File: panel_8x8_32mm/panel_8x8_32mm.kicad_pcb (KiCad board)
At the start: 2 copper layers, 32 x 32 mm, 17 parts, among them IC1 ATMEGA168-A, P1 CONN_8, P2 CONN_8, U1 ULN2804A, X1 CR

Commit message: consistent file naming
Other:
- board text added: "https://reiserlab.github.io/ Modular-LED-Display/"
- board text added: "panel 8x8 32mm v1.4 (2021)"
- board text removed: "Flypanel v1.3 (2012)"
- board text removed: "IO Rodeo Inc. (626) 793-8284"
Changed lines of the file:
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@@
     (visible_elements FFFFFF7F)
     (pcbplotparams
-      (layerselection 0x00030_ffffffff)
+      (layerselection 0x010f0_ffffffff)
       (usegerberextensions true)
       (usegerberattributes true)
@@
       (outputformat 1)
       (mirror false)
-      (drillshape 1)
+      (drillshape 0)
       (scaleselection 1)
-      (outputdirectory "gerber_v1p3/"))
+      (outputdirectory "production_v1/"))
   )
   (net 0 "")
@@
   (gr_line (start 99.9998 68.00088) (end 132.00126 68.00088) (angle 90) (layer Edge.Cuts) (width 0.381))
   (gr_line (start 99.9998 99.9998) (end 99.9998 68.00088) (angle 90) (layer Edge.Cuts) (width 0.381))
-  (gr_text "IO Rodeo Inc. (626) 793-8284" (at 100.89896 83.10118 90) (layer B.SilkS)
+  (gr_text "https://reiserlab.github.io/\nModular-LED-Display/" (at 116.52 70.55) (layer B.SilkS)
     (effects (font (size 1.00076 1.00076) (thickness 0.20066)) (justify mirror))
   )
-  (gr_text "Flypanel v1.3 (2012)" (at 116.0018 69.99986) (layer B.SilkS)
+  (gr_text "panel 8x8 32mm v1.4 (2021)" (at 101.3 84.52 90) (layer B.SilkS)
     (effects (font (size 1.00076 1.00076) (thickness 0.20066)) (justify mirror))
   )

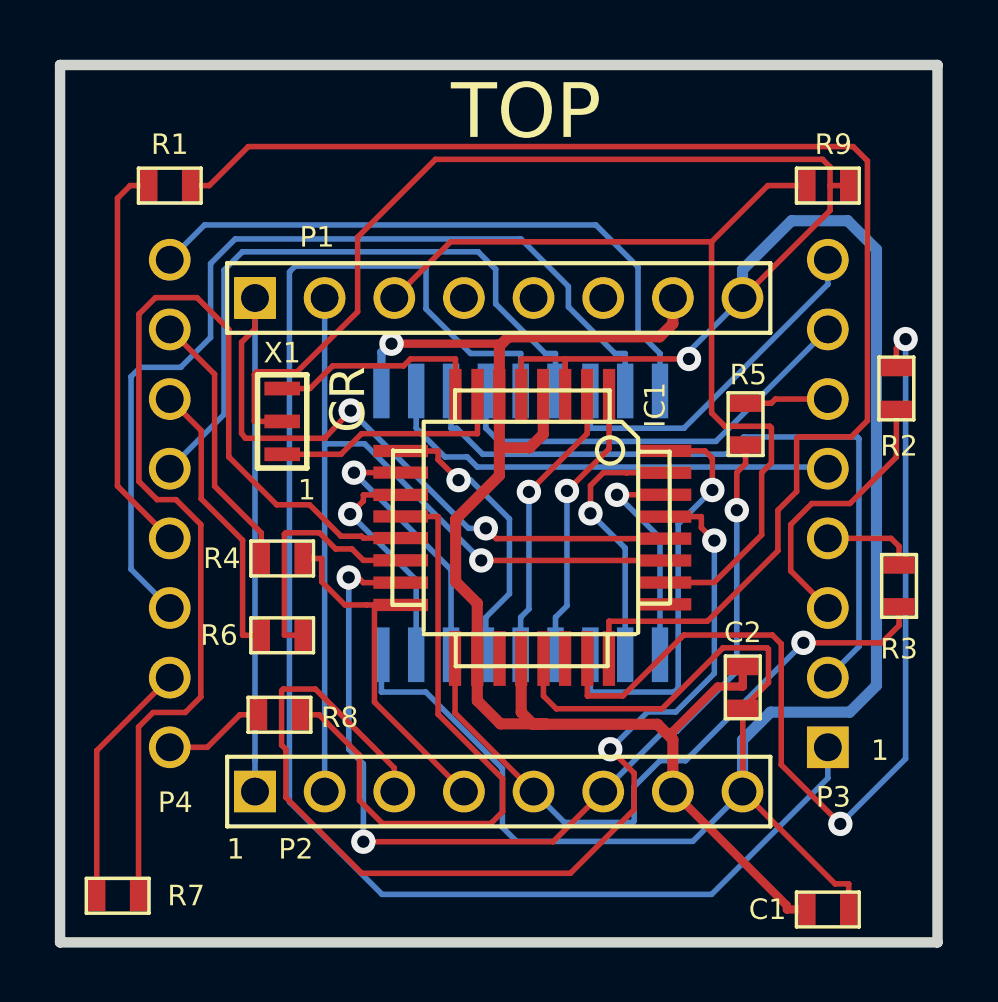
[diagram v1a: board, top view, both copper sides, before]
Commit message: migrate to KiCad 6
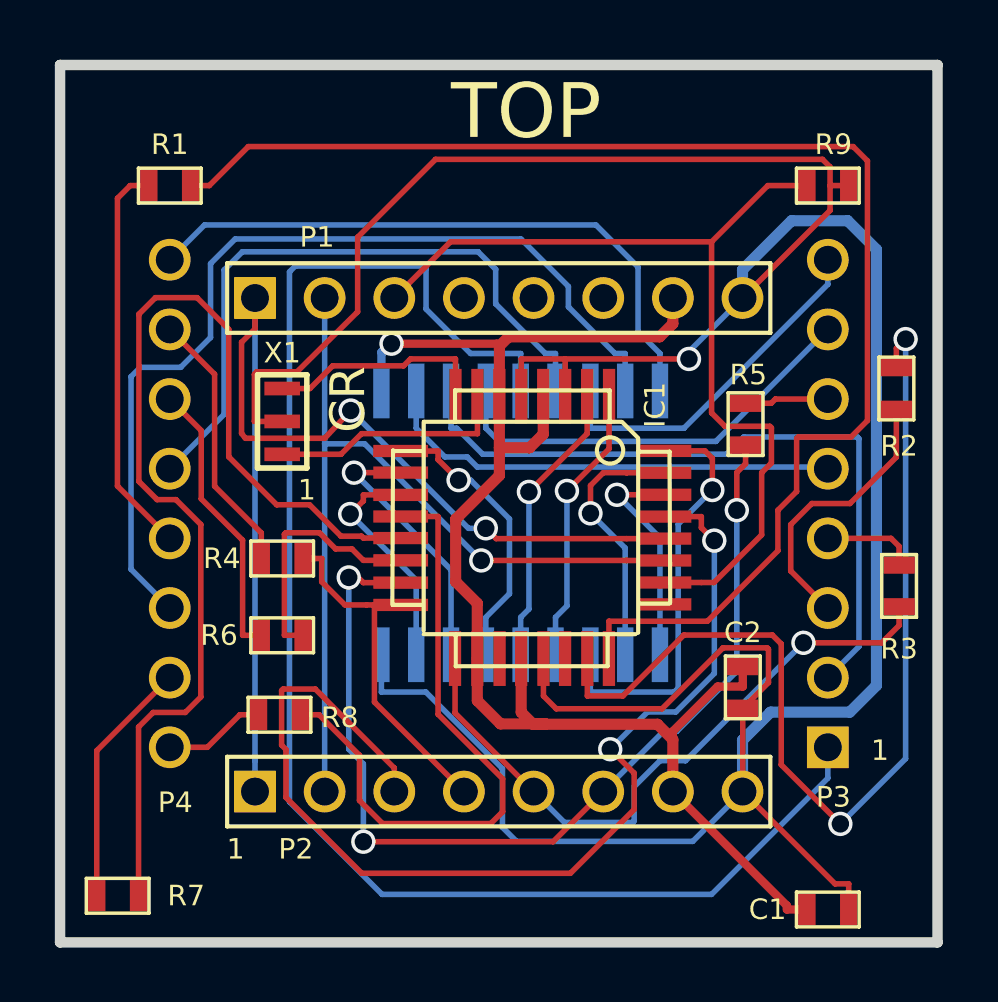
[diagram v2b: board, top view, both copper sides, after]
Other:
- net class Default removed
- net class VCC removed
